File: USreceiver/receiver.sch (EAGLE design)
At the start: 11 parts

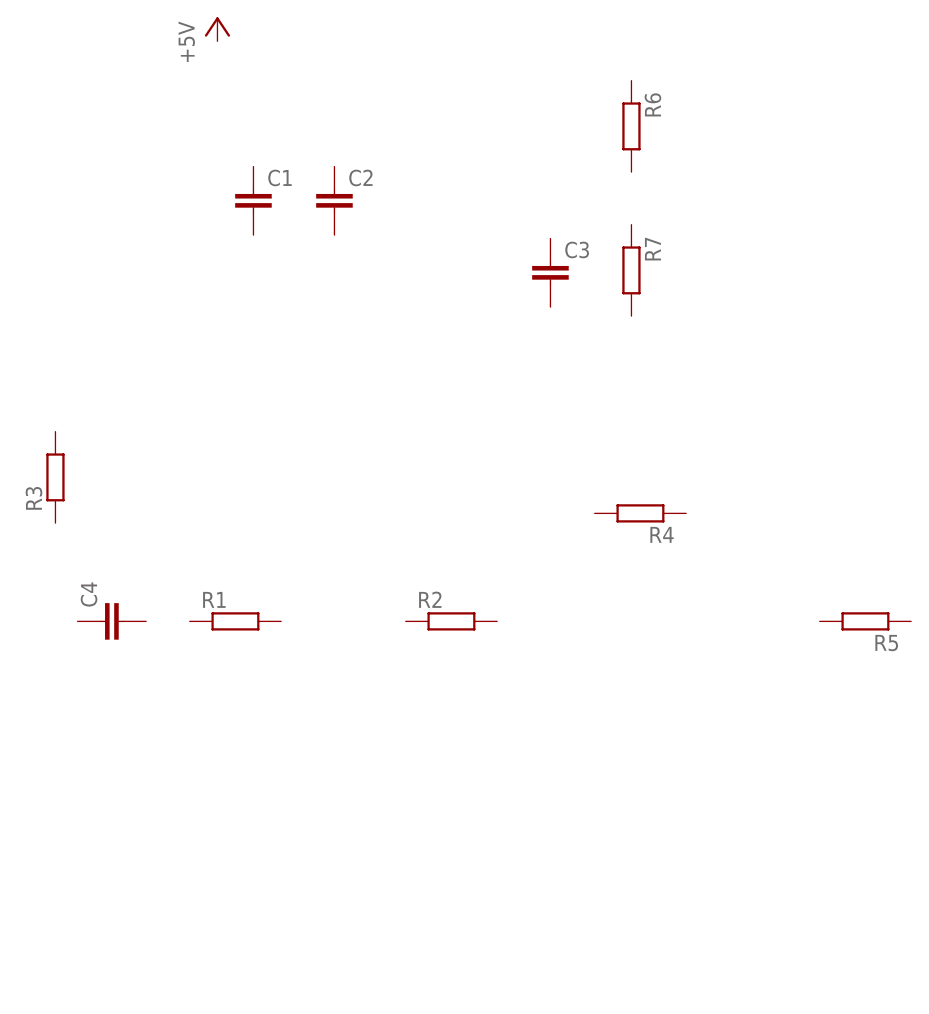
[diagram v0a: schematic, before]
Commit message: Added a new Amplifier
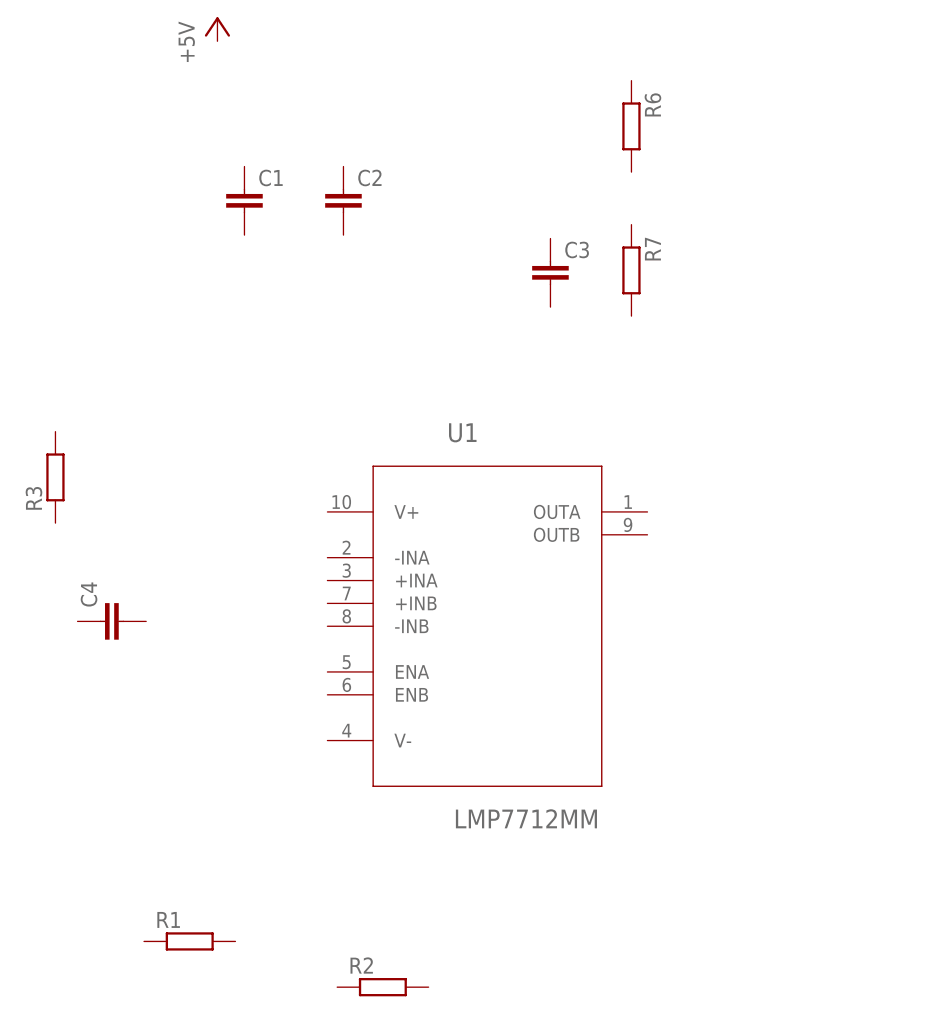
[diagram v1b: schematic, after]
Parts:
- removed R4, R5: (no value), resistor:R-EU_R0603
- added U1: LMP7712MM, libSheldonDrone:LMP7712MM
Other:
- moved on the sheet: C1, C2, R1, R2
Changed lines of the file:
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@@
 <?xml version="1.0" encoding="utf-8"?>
 <!DOCTYPE eagle SYSTEM "eagle.dtd">
-<eagle version="7.4.0">
+<eagle version="7.2.0">
 <drawing>
 <settings>
@@
 <setting verticaltext="up"/>
 </settings>
-<grid distance="1" unitdist="mm" unit="mm" style="lines" multiple="1" display="yes" altdistance="0.01" altunitdist="inch" altunit="inch"/>
+<grid distance="1" unitdist="mm" unit="mm" style="lines" multiple="1" display="no" altdistance="0.01" altunitdist="inch" altunit="inch"/>
 <layers>
 <layer number="1" name="Top" color="4" fill="1" visible="no" active="no"/>
@@
 <part name="R2" library="resistor" deviceset="R-EU_" device="R0603"/>
 <part name="R3" library="resistor" deviceset="R-EU_" device="R0603"/>
-<part name="R4" library="resistor" deviceset="R-EU_" device="R0603"/>
-<part name="R5" library="resistor" deviceset="R-EU_" device="R0603"/>
 <part name="R6" library="resistor" deviceset="R-EU_" device="R0603"/>
 <part name="R7" library="resistor" deviceset="R-EU_" device="R0603"/>
@@
 <part name="C3" library="resistor" deviceset="C-EU" device="C0603"/>
 <part name="C4" library="resistor" deviceset="C-EU" device="C0603"/>
+<part name="U1" library="libSheldonDrone" deviceset="LMP7712MM" device=""/>
 </parts>
 <sheets>
@@
 </plain>
 <instances>
-<instance part="R1" gate="G$1" x="19" y="27"/>
-<instance part="R2" gate="G$1" x="43" y="27"/>
+<instance part="R1" gate="G$1" x="13.92" y="-8.56"/>
+<instance part="R2" gate="G$1" x="35.38" y="-13.64"/>
 <instance part="R3" gate="G$1" x="-1" y="43" rot="R90"/>
-<instance part="R4" gate="G$1" x="64" y="39" rot="R180"/>
-<instance part="R5" gate="G$1" x="89" y="27" rot="R180"/>
 <instance part="R6" gate="G$1" x="63" y="82" rot="R270"/>
 <instance part="R7" gate="G$1" x="63" y="66" rot="R270"/>
 <instance part="P+1" gate="1" x="17" y="94"/>
-<instance part="C1" gate="G$1" x="21" y="75"/>
-<instance part="C2" gate="G$1" x="30" y="75"/>
+<instance part="C1" gate="G$1" x="20" y="75"/>
+<instance part="C2" gate="G$1" x="31" y="75"/>
 <instance part="C3" gate="G$1" x="54" y="67"/>
 <instance part="C4" gate="G$1" x="4" y="27" rot="R90"/>
+<instance part="U1" gate="A" x="47" y="29"/>
 </instances>
 <busses>

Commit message: Schematic done. Board started. Library updated.
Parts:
- added 100µ1: (no value), @Club_passif:CPOL_DIAM5MM
- added C10, C5, C6, C7, C8, C9: 100n, resistor:C-EUC0603
- added LED1: LED_3MM, @Club_passif:LED_3MM
- added R10, R12, R14, R15, R17, R19, R21, R23, R24, R25, R26, R4, R8, R9: (no value), resistor:R-EU_R0603
- added R11, R13, R16, R18, R20, R22, R5: 4,7k, resistor:R-EU_R0603
- added R27: 1k, resistor:R-EU_R0603
- added U$9: STM32-H103, libSheldonDrone:STM32-H103
- added U2, U3, U4: LMP7712MM, libSheldonDrone:LMP7712MM
- added U5: LM1117MP-3.3, libSheldonDrone:LM1117MP-3.3
- added US1_U1, US1_U2, US1_U3, US1_U4, US2_U1, US2_U2, US2_U3, US2_U4: US-R-10MM, libSheldonDrone:US-R-10MM
- C1, C2, C3, C4: value (none) -> 100n
- R3: value (none) -> 4,7k
- R6, R7: value (none) -> 1k
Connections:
- new net +3V3: C2.1, R11.2, R13.2, R16.2, R18.2, R20.2, R22.2, R3.2, R5.2, R6.1, U1.V+, U2.V+, U3.V+, U4.V+, U5.OUT
- new net +5V: 100µ1.P$1, C10.1, U$9.+5V_USB, U5.IN
- new net GND: 100µ1.P$2, C10.2, C2.2, R27.2, R7.2, U$9.GND@1, U$9.GND@2, U$9.GND@3, U1.V-, U2.V-, U3.V-, U4.V-, U5.ADJ/GND, U5.VOUT, US1_U1.P$2, US1_U2.P$2, US1_U3.P$2, US1_U4.P$2, US2_U1.P$2, US2_U2.P$2, US2_U3.P$2, US2_U4.P$2
- new net N$1: C1.1, R11.1, US1_U2.P$1
- new net N$10: C6.2, R15.1
- new net N$11: C7.1, R18.1, US2_U3.P$1
- new net N$12: C7.2, R17.1
- new net N$13: C8.1, R20.1, US1_U4.P$1
- new net N$14: C8.2, R19.1
- new net N$15: C9.1, R22.1, US2_U4.P$1
- new net N$16: C9.2, R21.1
- new net N$17: LED1.A, U$9.PA1
- new net N$18: LED1.C, R27.1
- new net N$2: C1.2, R9.1
- new net N$3: C4.1, R3.1, US1_U1.P$1
- new net N$4: C4.2, R1.1
- new net N$5: C5.1, R5.1, US2_U1.P$1
- new net N$6: C5.2, R4.1
- new net N$7: C3.1, R13.1, US2_U2.P$1
- new net N$8: C3.2, R12.1
- new net N$9: C6.1, R16.1, US1_U3.P$1
- new net S1: R8.2, U$9.PC0, U1.OUTA
- new net S2: R2.1, U$9.PC1, U1.OUTB
- new net S3: R14.2, U$9.PC2, U2.OUTA
- new net S4: R10.1, U$9.PC3, U2.OUTB
- new net S5: R24.2, U$9.PC4/USB-P, U3.OUTA
- new net S6: R23.1, U$9.PC5, U3.OUTB
- new net S7: R26.2, U$9.PB0, U4.OUTA
- new net S8: R25.1, U$9.PB1, U4.OUTB
- new net U1A-: R1.2, R8.1, U1.-INA
- new net U1B-: R2.2, R4.2, U1.-INB
- new net U2A-: R14.1, R9.2, U2.-INA
- new net U2B-: R10.2, R12.2, U2.-INB
- new net U3A-: R15.2, R24.1, U3.-INA
- new net U3B-: R17.2, R23.2, U3.-INB
- new net U4A-: R19.2, R26.1, U4.-INA
- new net U4B-: R21.2, R25.2, U4.-INB
- new net VCC/2: R6.2, R7.1, U1.+INA, U1.+INB, U2.+INA, U2.+INB, U3.+INA, U3.+INB, U4.+INA, U4.+INB
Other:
- note added: "Olimex board"
- note added: "Sheldon Project 2015"
- note added: "Supply"
- note added: "US Receiver and amplification"
- moved on the sheet: C1, C2, C3, C4, R1, R2, R3, R6, R7, U1

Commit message: Board finished
Board design is finished, pictures are exported. Ready to be sent in
fab.
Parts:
- added C12, C13: 2.2µ, @Club_passif:CPOL_DIAM5MM
- C11: value (none) -> 100µ
- R1, R12, R15, R17, R19, R21, R4, R9: value (none) -> 1k
- R10, R14, R2, R23, R24, R25, R26, R8: value (none) -> 100k
- renumbered 100µ1 to C11
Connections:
- net +3V3: now also C12.P$1
- net GND: now also C12.P$2, C13.P$2
- net VCC/2: now also C13.P$1
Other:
- moved on the sheet: C2, R6, R7
